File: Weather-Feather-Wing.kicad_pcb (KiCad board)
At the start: 4 copper layers, 50.8 x 22.9 mm, 35 parts, among them J2 Conn_01x16, J3 Conn_01x12, Q1 BSS138, U1 AP2112K-3.3, U2 SHT4x, U3 SCD41-D-R2, U4 BMP390, U5 SGP40-D-R4

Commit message: Corrections and improvements.
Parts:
- C8, C9: value 0.1uF -> 1uF
- R7: value 10K -> 4.7
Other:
- outline, holes or cut-outs redrawn
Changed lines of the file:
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@@
 			(dashed_line_gap_ratio 3.000000)
 			(svgprecision 4)
-			(plotframeref yes)
+			(plotframeref no)
 			(mode 1)
 			(useauxorigin no)
@@
 			)
 		)
-		(property "Value" "0.1uF"
+		(property "Value" "1uF"
 			(at 0 1.43 90)
 			(layer "F.Fab")
@@
 			)
 		)
-		(property "Value" "10K"
+		(property "Value" "4.7"
 			(at 0 1.43 0)
 			(layer "F.Fab")
@@
 			)
 		)
-		(property "Value" "0.1uF"
+		(property "Value" "1uF"
 			(at 0 1.43 90)
 			(layer "F.Fab")
@@
 	)
 	(gr_line
-		(start 203.2 101.6)
-		(end 203.2 124.46)
+		(start 203.2 104.14)
+		(end 203.2 121.92)
 		(stroke
-			(width 0.0508)
+			(width 0.05)
 			(type solid)
 		)
@@
 	)
 	(gr_line
-		(start 152.4 124.46)
-		(end 152.4 101.6)
+		(start 152.4 121.92)
+		(end 152.4 104.14)
 		(stroke
-			(width 0.0508)
+			(width 0.05)
 			(type solid)
 		)
@@
 		(layer "Edge.Cuts")
 	)
+	(gr_arc
+		(start 152.4 104.14)
+		(mid 153.143949 102.343949)
+		(end 154.94 101.6)
+		(stroke
+			(width 0.05)
+			(type default)
+		)
+		(layer "Edge.Cuts")
+	)
+	(gr_arc
+		(start 203.2 121.92)
+		(mid 202.456051 123.716051)
+		(end 200.66 124.46)
+		(stroke
+			(width 0.05)
+			(type default)
+		)
+		(layer "Edge.Cuts")
+	)
 	(gr_line
-		(start 152.4 101.6)
-		(end 203.2 101.6)
+		(start 154.94 101.6)
+		(end 200.66 101.6)
 		(stroke
-			(width 0.0508)
+			(width 0.05)
 			(type solid)
 		)
@@
 	)
 	(gr_line
-		(start 203.2 124.46)
-		(end 152.4 124.46)
+		(start 200.66 124.46)
+		(end 154.94 124.46)
 		(stroke
-			(width 0.0508)
+			(width 0.05)
 			(type solid)
 		)
 		(layer "Edge.Cuts")
+	)
+	(gr_arc
+		(start 200.66 101.6)
+		(mid 202.456051 102.343949)
+		(end 203.2 104.14)
+		(stroke
+			(width 0.05)
+			(type default)
+		)
+		(layer "Edge.Cuts")
+	)
+	(gr_arc
+		(start 154.94 124.46)
+		(mid 153.143949 123.716051)
+		(end 152.4 121.92)
+		(stroke
+			(width 0.05)
+			(type default)
+		)
+		(layer "Edge.Cuts")

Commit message: As ordered from OSH Park.
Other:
- board text added: "WEATHER FEATHER WING DESIGNED BY BEN CROCKETT SHT4x: 0x44 BMP390: 0x77 SGP4x: 0x59 BMP581: 0x47 SCD4x: 0x62"
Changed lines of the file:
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@@
 		(layer "Edge.Cuts")
+	)
+	(gr_text "WEATHER FEATHER WING\nDESIGNED BY BEN CROCKETT\n\nSHT4x: 0x44		BMP390: 0x77\nSGP4x: 0x59		BMP581: 0x47\nSCD4x: 0x62"
+		(at 194.5386 109.22 0)
+		(layer "B.SilkS")
+		(effects
+			(font
+				(size 1 1)
+				(thickness 0.15)
+			)
+			(justify left top mirror)
+		)
 	)
 	(dimension

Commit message: Cleanup and updates
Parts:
- H1, H2, H3, H4: footprint Adafruit BMP390:FEATHER_MOUNTING_HOLE_2.5_PLATED -> TI_MSPM0_DSBGA:MOUNTINGHOLE_2.5_PLATED
- J5: renamed from CONN1; value STEMMA_I2C_QT -> JST_SH4; footprint Adafruit SHT45:JST_SH4 -> Weather_Feather:JST_SH4
- J6: renamed from CONN2; value STEMMA_I2C_QT -> JST_SH4; footprint Adafruit SHT45:JST_SH4 -> Weather_Feather:JST_SH4
- U2: footprint Adafruit SHT45:SHT4X -> Weather_Feather:SHT4X
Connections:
- J2 pad 11: unconnected-(J2-Pin_11-Pad11) -> /SCK_Feather
- J2 pad 12: unconnected-(J2-Pin_12-Pad12) -> /MO_Feather
- J2 pad 13: unconnected-(J2-Pin_13-Pad13) -> /MI_Feather

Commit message: Updates after building the board.
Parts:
- D1: footprint Adafruit SHT45:CHIPLED_0603_NOOUTLINE -> LED_SMD:LED_0603_1608Metric_Pad1.05x0.95mm_HandSolder
- J1: renamed from J5; footprint Weather_Feather:JST_SH4 -> Weather_Feather:JST_SH_SM04B-SRSS-TB_1x04-1MP_P1.00mm_Horizontal
- J2: renamed from J6; footprint Weather_Feather:JST_SH4 -> Weather_Feather:JST_SH_SM04B-SRSS-TB_1x04-1MP_P1.00mm_Horizontal
- U1: footprint Adafruit SHT45:SOT23-5 -> Weather_Feather:SOT23-5
- turned D1 to 0 degrees
- turned U1 to 0 degrees
- renumbered J2 to J3, J3 to J4
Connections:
- R1 pad 2: Net-(D1-PadA) -> Net-(D1-A)
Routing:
- net GND: track 39.4 -> 42.1 mm, vias 21 -> 25
- net Net-(D1-PadA): track 2.50 -> 0.00 mm
- net Net-(D1-A): track 0.00 -> 2.37 mm
- net /SDA_3V: track 92.9 -> 94.2 mm
- net /SCL: track 65.0 -> 65.6 mm
- added copper zone on In2.Cu, net +3.3V
- added copper zone on In1.Cu, net GND
- removed copper zone on In1.Cu, net +3.3V
- removed copper zone on In2.Cu, net GND
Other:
- board text added: "WEATHER FEATHER WING BY BEN CROCKETT SHT4x: 0x44 BMP390: 0x77 SGP4x: 0x59 BMP581: 0x47 SCD4x: 0x62"
- board text removed: "WEATHER FEATHER WING DESIGNED BY BEN CROCKETT SHT4x: 0x44 BMP390: 0x77 SGP4x: 0x59 BMP581: 0x47 SCD4x: 0x62"

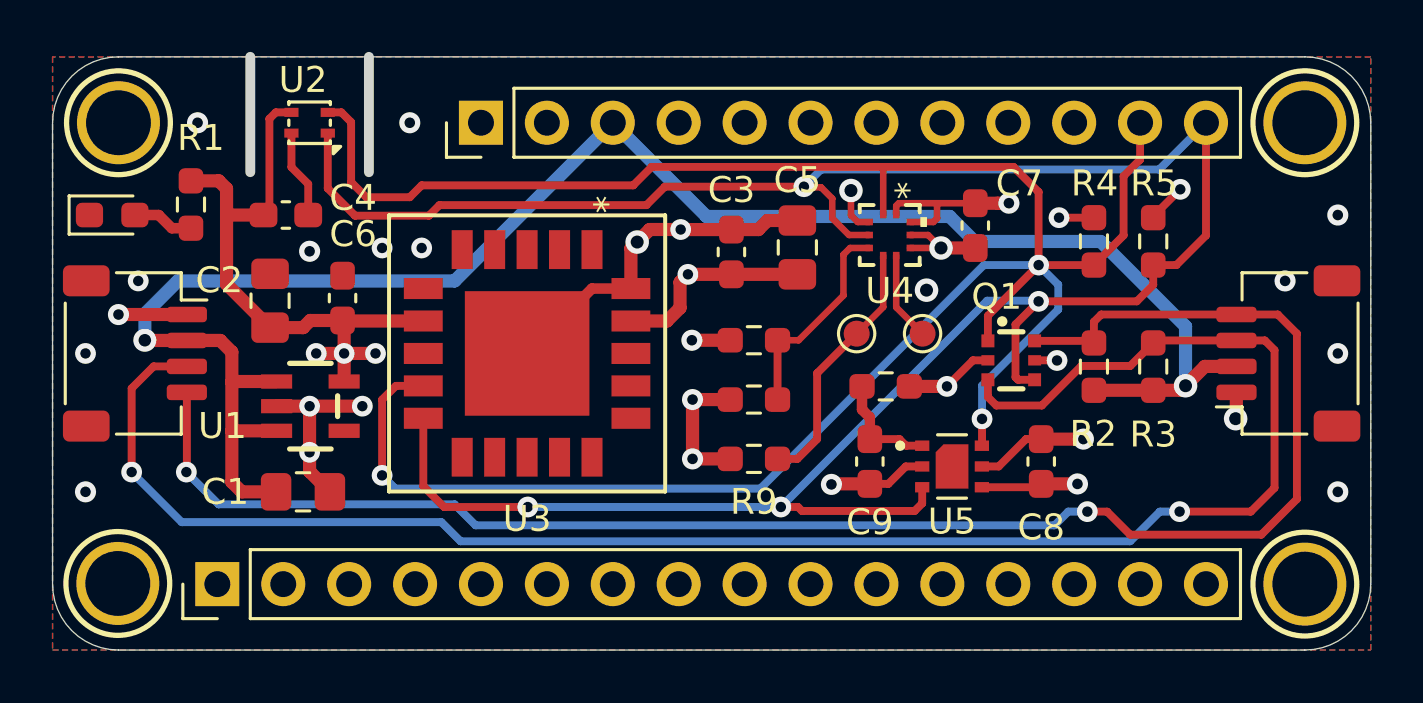
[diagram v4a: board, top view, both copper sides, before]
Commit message: Design corrections, moved both header pins 50 mils closer to their respective edges.
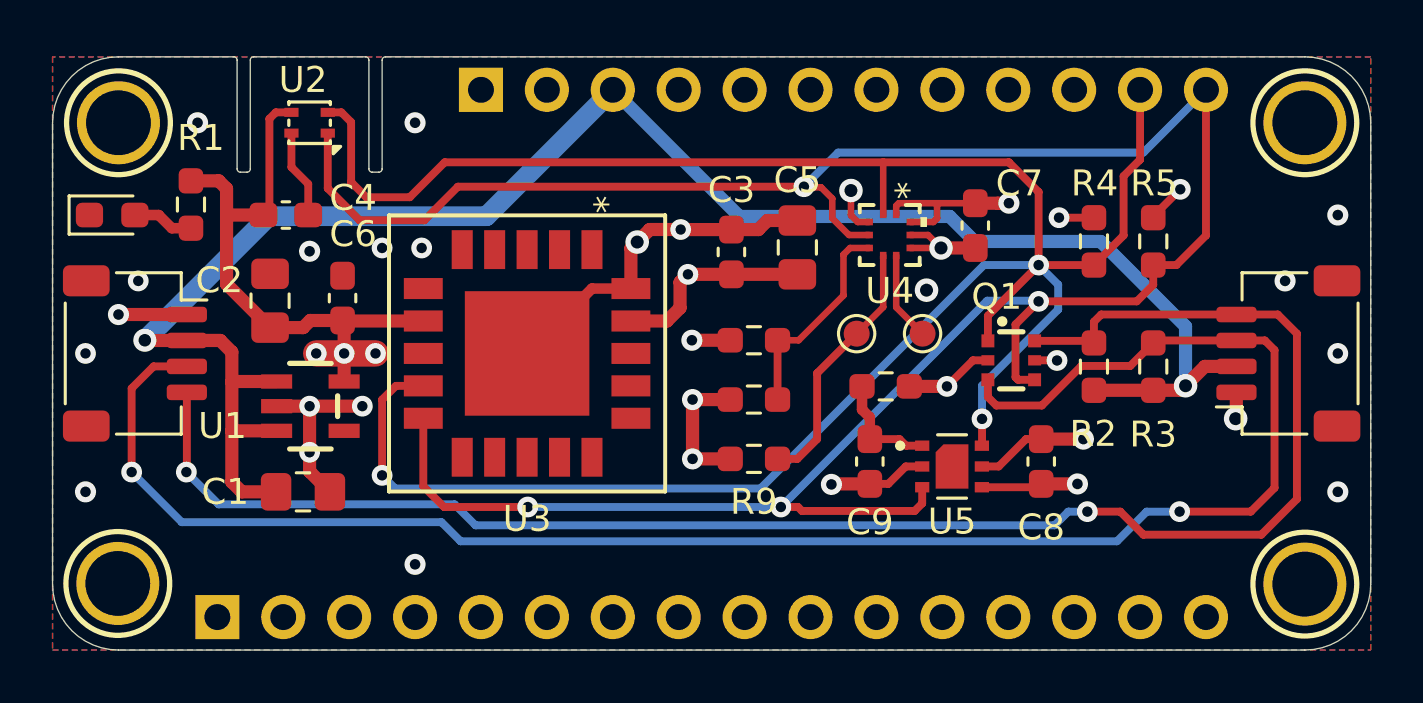
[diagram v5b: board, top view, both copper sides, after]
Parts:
- J3: footprint Connector_PinHeader_2.54mm:PinHeader_1x16_P2.54mm_Vertical -> Weather_Feather:PinHeader_1x16_P2.54mm_Vertical
- J4: footprint Connector_PinHeader_2.54mm:PinHeader_1x12_P2.54mm_Vertical -> Weather_Feather:PinHeader_1x12_P2.54mm_Vertical
- moved J3 1.27 mm to (158.8, 123.2)
- moved J4 1.27 mm to (168.9, 102.9)
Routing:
- net GND: track 42.1 -> 44.2 mm, vias 25 -> 26
- net /SDA_3V: track 94.2 -> 96.2 mm
- net /SCL_3V: track 90.0 -> 91.6 mm
- added copper zone on In1.Cu, net +3.3V
- added copper zone on In2.Cu, net GND
- removed copper zone on In2.Cu, net +3.3V
- removed copper zone on In1.Cu, net GND
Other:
- outline, holes or cut-outs redrawn
